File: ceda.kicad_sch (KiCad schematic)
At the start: 0 parts

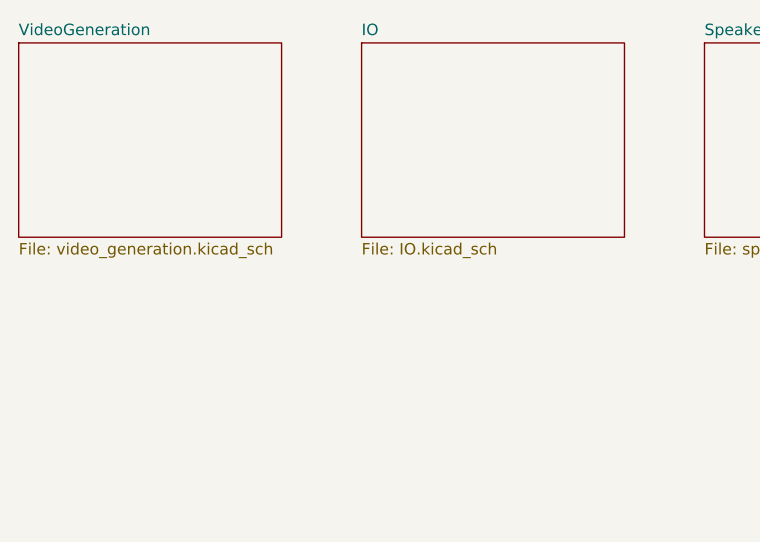
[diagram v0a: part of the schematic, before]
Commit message: Embed new sheets and fix symbols.
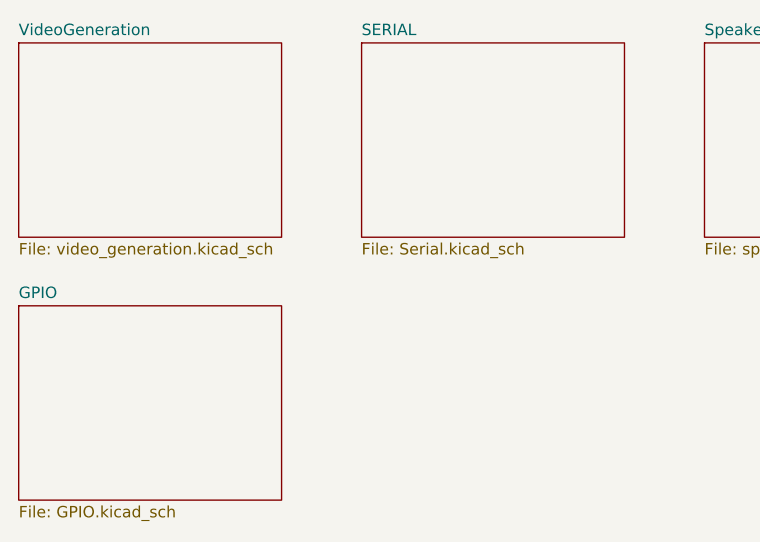
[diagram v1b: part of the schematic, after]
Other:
- sheet IO renamed SERIAL
- added sheet GPIO (GPIO.kicad_sch)
- sheet SERIAL: file IO.kicad_sch -> Serial.kicad_sch
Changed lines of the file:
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@@
+    )
+  )
+  (sheet (at 25.4 54.61) (size 29.21 21.59) (fields_autoplaced)
+    (stroke (width 0.1524) (type solid) (color 0 0 0 0))
+    (fill (color 0 0 0 0.0000))
+    (property "Sheet name" "GPIO" (id 0) (at 25.4 53.8984 0)
+      (effects (font (size 1.27 1.27)) (justify left bottom))
+    )
+    (property "Sheet file" "GPIO.kicad_sch" (id 1) (at 25.4 76.7846 0)
+      (effects (font (size 1.27 1.27)) (justify left top))
     )
   )
@@
     (stroke (width 0.1524) (type solid) (color 0 0 0 0))
     (fill (color 0 0 0 0.0000))
-    (property "Sheet name" "IO" (id 0) (at 63.5 24.6884 0)
+    (property "Sheet name" "SERIAL" (id 0) (at 63.5 24.6884 0)
       (effects (font (size 1.27 1.27)) (justify left bottom))
     )
-    (property "Sheet file" "IO.kicad_sch" (id 1) (at 63.5 47.5746 0)
+    (property "Sheet file" "Serial.kicad_sch" (id 1) (at 63.5 47.5746 0)
       (effects (font (size 1.27 1.27)) (justify left top))
     )
@@
     (path "/ef850a34-fb31-4ec2-8b90-4e6ea535ae17" (page "4"))
     (path "/1847fdc4-53d8-4940-8c5f-7a326599bae2" (page "5"))
+    (path "/23c42ab9-740a-4e84-88f1-9f74965e7273" (page "6"))
   )
   (symbol_instances
@@
       (reference "#PWR?") (unit 1) (value "GND") (footprint "")
     )
+    (path "/23c42ab9-740a-4e84-88f1-9f74965e7273/3eef50a5-c9f6-4380-8968-412e4e210646"
+      (reference "#PWR?") (unit 1) (value "GND") (footprint "")
+    )
     (path "/ce60e45b-d802-4380-8f39-bef3de5fa20e/44904acb-380f-449a-b553-049731fee477"
       (reference "#PWR?") (unit 1) (value "VCC") (footprint "")
@@
     (path "/ce60e45b-d802-4380-8f39-bef3de5fa20e/4f72cf7f-9018-4e80-b599-22f4012bbe5a"
       (reference "#PWR?") (unit 1) (value "VCC") (footprint "")
+    )
+    (path "/23c42ab9-740a-4e84-88f1-9f74965e7273/4f79b821-bb86-4a79-8cc9-a31ff99ad1b3"
+      (reference "#PWR?") (unit 1) (value "GND") (footprint "")
     )
     (path "/ef850a34-fb31-4ec2-8b90-4e6ea535ae17/526bc8fc-b9ea-4f6d-a11e-04b82edc0316"
@@
       (reference "#PWR?") (unit 1) (value "GND") (footprint "")
     )
+    (path "/23c42ab9-740a-4e84-88f1-9f74965e7273/81f6af90-205c-4009-9fca-95e76bc3a30c"
+      (reference "#PWR?") (unit 1) (value "GND") (footprint "")
+    )
     (path "/ce60e45b-d802-4380-8f39-bef3de5fa20e/8708e44f-744a-4c71-8d3e-9b33e5565dd3"
       (reference "#PWR?") (unit 1) (value "GND") (footprint "")
@@
     (path "/1847fdc4-53d8-4940-8c5f-7a326599bae2/ac0df0c0-bf3f-4c2e-9fcf-2dcb79aa226c"
       (reference "#PWR?") (unit 1) (value "GND") (footprint "")
+    )
+    (path "/23c42ab9-740a-4e84-88f1-9f74965e7273/acd3b74a-4ce0-4828-b235-d3353f238170"
+      (reference "#PWR?") (unit 1) (value "VCC") (footprint "")
     )
     (path "/ce60e45b-d802-4380-8f39-bef3de5fa20e/afa3161e-0796-4f88-bb71-3bac43397641"
@@
       (reference "#PWR?") (unit 1) (value "GND") (footprint "")
     )
+    (path "/23c42ab9-740a-4e84-88f1-9f74965e7273/be6090c6-9d5f-45e2-8095-8eb5a1703aa2"
+      (reference "#PWR?") (unit 1) (value "VCC") (footprint "")
+    )
     (path "/ef850a34-fb31-4ec2-8b90-4e6ea535ae17/bfe7a632-2cca-4194-b346-5928404f8228"
       (reference "#PWR?") (unit 1) (value "GND") (footprint "")
@@
       (reference "#PWR?") (unit 1) (value "GND") (footprint "")
     )
+    (path "/23c42ab9-740a-4e84-88f1-9f74965e7273/f7eb22af-aba2-4009-a993-e9895948b84e"
+      (reference "#PWR?") (unit 1) (value "VCC") (footprint "")
+    )
     (path "/ce60e45b-d802-4380-8f39-bef3de5fa20e/f9799c5d-8034-46e6-ad18-7f272051b29a"
       (reference "#PWR?") (unit 1) (value "VCC") (footprint "")
@@
     (path "/1847fdc4-53d8-4940-8c5f-7a326599bae2/fada5dd4-0d0e-47e0-a18d-0bc406ca8606"
       (reference "#PWR?") (unit 1) (value "VCC") (footprint "")
+    )
+    (path "/23c42ab9-740a-4e84-88f1-9f74965e7273/b4e68656-41c0-4812-b001-a90783a3a6bd"
+      (reference "B10-B14") (unit 1) (value "uPD8255") (footprint "")
     )
     (path "/e6a0e8fd-e32c-428e-9a73-cac8f5494d05/e3df07bf-3ffc-4940-820c-1edcc7f8802c"
@@
       (reference "E13") (unit 1) (value "74LS04") (footprint "")
     )
+    (path "/23c42ab9-740a-4e84-88f1-9f74965e7273/1d67d68b-66f8-4965-a562-05de77bcd7e5"
+      (reference "E13") (unit 2) (value "74LS04") (footprint "")
+    )
     (path "/ce60e45b-d802-4380-8f39-bef3de5fa20e/24d193cd-79a4-4ad8-8472-2b96f466d141"
       (reference "E13") (unit 4) (value "74LS04") (footprint "")
     )
+    (path "/23c42ab9-740a-4e84-88f1-9f74965e7273/24147921-68ae-4eb7-94fb-991f083e4eb0"
+      (reference "E14") (unit 2) (value "74LS74") (footprint "")
+    )
     (path "/1847fdc4-53d8-4940-8c5f-7a326599bae2/4f4ed95e-9189-46b4-888b-34cae86c7a4c"
       (reference "F2-F5") (unit 1) (value "Z80CPU") (footprint "")
@@
       (reference "F10") (unit 1) (value "74LS157") (footprint "")
     )
+    (path "/23c42ab9-740a-4e84-88f1-9f74965e7273/b2cb7d22-ca6e-4a29-949e-c29c143ac78c"
+      (reference "F13") (unit 2) (value "74LS08") (footprint "")
+    )
+    (path "/23c42ab9-740a-4e84-88f1-9f74965e7273/2f3af18b-1450-45cc-b2c4-93c8e85c8548"
+      (reference "F13") (unit 3) (value "74LS08") (footprint "")
+    )
+    (path "/23c42ab9-740a-4e84-88f1-9f74965e7273/03a4a81b-4d50-433c-ac26-4ba879c2eeff"
+      (reference "F14") (unit 2) (value "74LS00") (footprint "")
+    )
+    (path "/23c42ab9-740a-4e84-88f1-9f74965e7273/4ce003b7-7093-412b-af0a-951a986e5231"
+      (reference "F14") (unit 3) (value "74LS00") (footprint "")
+    )
+    (path "/23c42ab9-740a-4e84-88f1-9f74965e7273/c182f1fe-96b2-41c4-9f23-e8cec8bd9e21"
+      (reference "F14") (unit 4) (value "74LS00") (footprint "")
+    )
     (path "/ce60e45b-d802-4380-8f39-bef3de5fa20e/5f190ef2-1902-4f45-a247-a0f33f417382"
       (reference "H8H10") (unit 1) (value "uPD446") (footprint "")
     )
+    (path "/23c42ab9-740a-4e84-88f1-9f74965e7273/837dc2df-09af-4d71-9a02-297b79a158e0"
+      (reference "H9") (unit 1) (value "uPD446") (footprint "")
+    )
     (path "/ce60e45b-d802-4380-8f39-bef3de5fa20e/626b8579-fdf0-471a-93e7-d48f3b78ace4"
       (reference "H11") (unit 1) (value "74LS273") (footprint "")
@@
       (reference "H12H14") (unit 1) (value "2732") (footprint "")
     )
+    (path "/23c42ab9-740a-4e84-88f1-9f74965e7273/88ee6807-a5cd-4e50-9da6-34d72ca7c3ae"
+      (reference "J9") (unit 1) (value "uPD446") (footprint "")
+    )
     (path "/ce60e45b-d802-4380-8f39-bef3de5fa20e/1345e9a3-3879-41b5-b386-9d3dc565dea0"

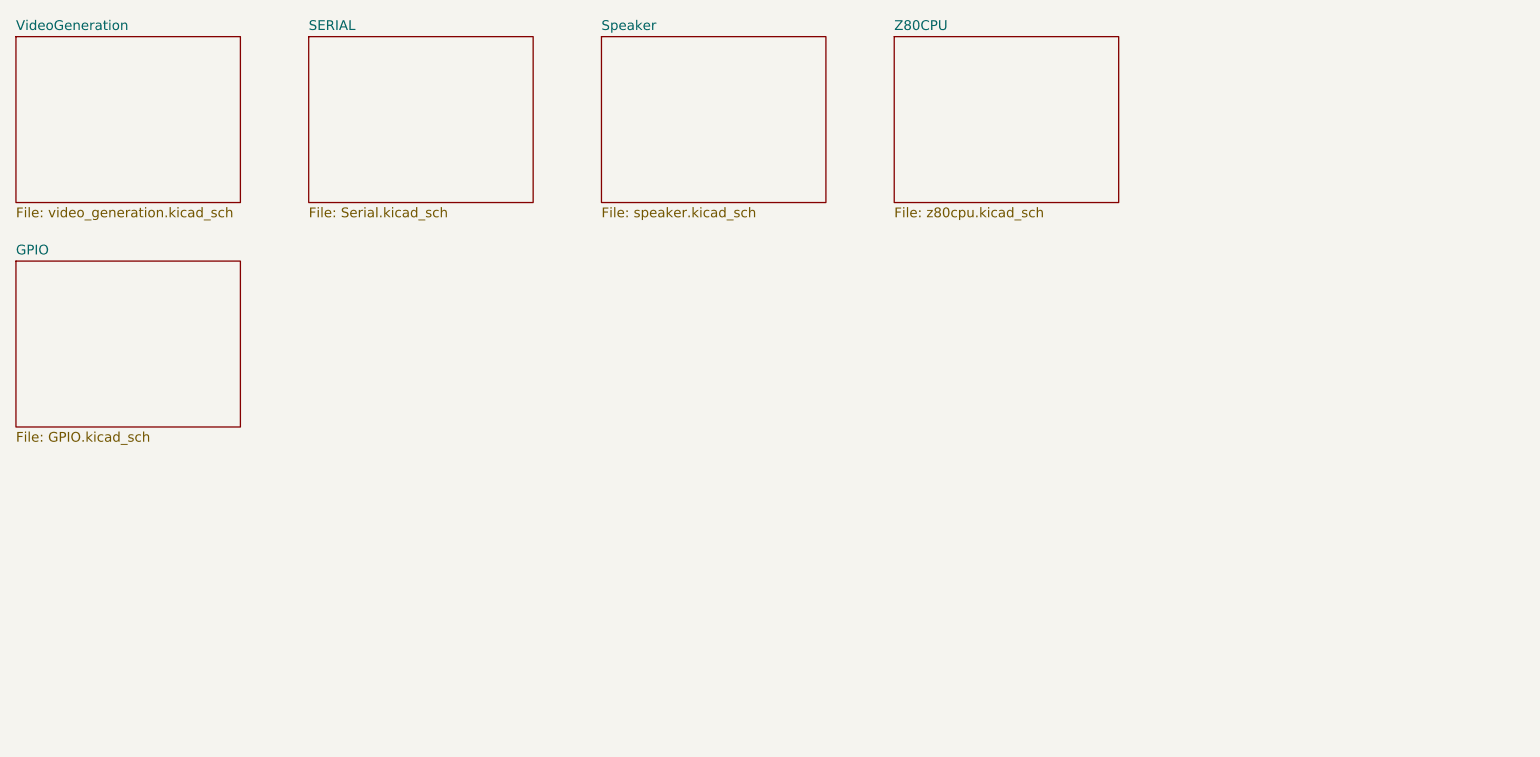
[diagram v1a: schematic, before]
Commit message: Add daughterboard schematics.
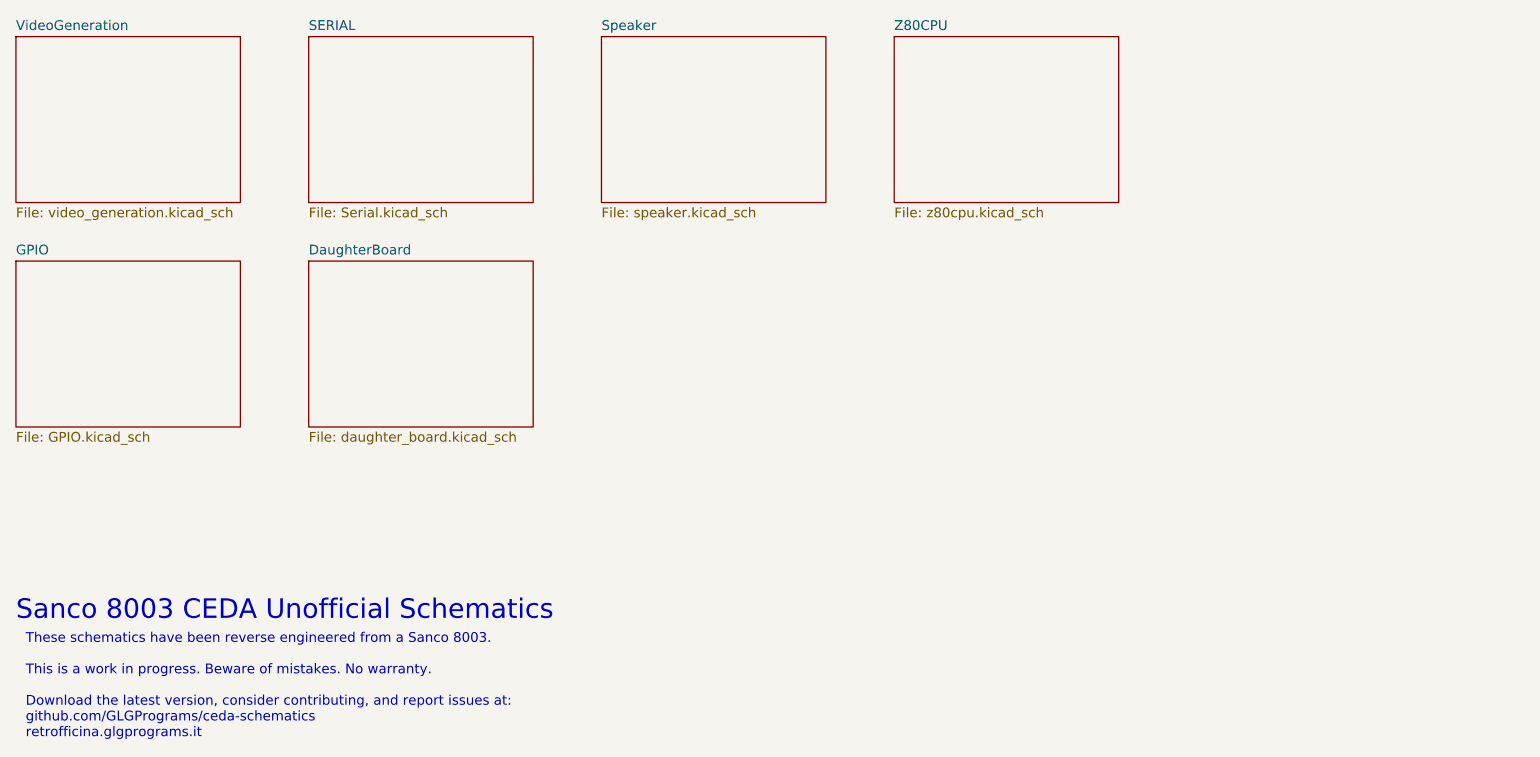
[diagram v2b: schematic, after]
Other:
- added sheet DaughterBoard (daughter_board.kicad_sch)
- note added: "Sanco 8003 CEDA Unofficial Schematics"
- note added: "These schematics have been reverse engineered from a Sanco 8003. This is a work in progress. Beware of mistakes. No warranty. Download the latest version, consider contributing, and report issues at: github.com/GLGPrograms/ceda-schematics retrofficina.glgprograms.it"
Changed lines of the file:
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@@
     (company "Logic Systems Int'l Inc")
   )
+  (text "These schematics have been reverse engineered from a Sanco 8003.\n\nThis is a work in progress. Beware of mistakes. No warranty.\n\nDownload the latest version, consider contributing, and report issues at:\ngithub.com/GLGPrograms/ceda-schematics\nretrofficina.glgprograms.it\n"
+    (at 26.67 116.84 0)
+    (effects (font (size 1.27 1.27)) (justify left bottom))
+  )
+  (text "Sanco 8003 CEDA Unofficial Schematics" (at 25.4 101.6 0)
+    (effects (font (size 2.54 2.54)) (justify left bottom))
+  )
   (sheet (at 139.7 25.4) (size 29.21 21.59) (fields_autoplaced)
     (stroke (width 0.1524) (type solid) (color 0 0 0 0))
@@
     )
     (property "Sheet file" "GPIO.kicad_sch" (id 1) (at 25.4 76.7846 0)
+      (effects (font (size 1.27 1.27)) (justify left top))
+    )
+  )
+  (sheet (at 63.5 54.61) (size 29.21 21.59) (fields_autoplaced)
+    (stroke (width 0.1524) (type solid) (color 0 0 0 0))
+    (fill (color 0 0 0 0.0000))
+    (property "Sheet name" "DaughterBoard" (id 0) (at 63.5 53.8984 0)
+      (effects (font (size 1.27 1.27)) (justify left bottom))
+    )
+    (property "Sheet file" "daughter_board.kicad_sch" (id 1) (at 63.5 76.7846 0)
       (effects (font (size 1.27 1.27)) (justify left top))
     )
@@
     (path "/1847fdc4-53d8-4940-8c5f-7a326599bae2" (page "5"))
     (path "/23c42ab9-740a-4e84-88f1-9f74965e7273" (page "6"))
+    (path "/4f1cc97c-1ae7-488a-96b4-ad54fee0fde4" (page "7"))
   )
   (symbol_instances
@@
       (reference "#PWR?") (unit 1) (value "+5V") (footprint "")
     )
+    (path "/4f1cc97c-1ae7-488a-96b4-ad54fee0fde4/3b12c81f-af2a-4545-b47f-dc7e2eccd6fa"
+      (reference "#PWR?") (unit 1) (value "VCC") (footprint "")
+    )
     (path "/1847fdc4-53d8-4940-8c5f-7a326599bae2/3bf4194b-f9e0-4505-8c24-68f9aad2fbc3"
       (reference "#PWR?") (unit 1) (value "GND") (footprint "")
@@
       (reference "#PWR?") (unit 1) (value "GND") (footprint "")
     )
+    (path "/4f1cc97c-1ae7-488a-96b4-ad54fee0fde4/43f7d1da-dc41-4737-81e0-b5bb678885e3"
+      (reference "#PWR?") (unit 1) (value "GND") (footprint "")
+    )
     (path "/ce60e45b-d802-4380-8f39-bef3de5fa20e/44904acb-380f-449a-b553-049731fee477"
       (reference "#PWR?") (unit 1) (value "VCC") (footprint "")
@@
       (reference "#PWR?") (unit 1) (value "VCC") (footprint "")
     )
+    (path "/4f1cc97c-1ae7-488a-96b4-ad54fee0fde4/4d2c484e-3a46-4211-852c-d4b4069e05ce"
+      (reference "#PWR?") (unit 1) (value "VCC") (footprint "")
+    )
+    (path "/4f1cc97c-1ae7-488a-96b4-ad54fee0fde4/4de7529a-3ebb-492a-9d76-afc139699f2f"
+      (reference "#PWR?") (unit 1) (value "GND") (footprint "")
+    )
     (path "/ce60e45b-d802-4380-8f39-bef3de5fa20e/4f72cf7f-9018-4e80-b599-22f4012bbe5a"
       (reference "#PWR?") (unit 1) (value "VCC") (footprint "")
@@
     (path "/ef850a34-fb31-4ec2-8b90-4e6ea535ae17/526bc8fc-b9ea-4f6d-a11e-04b82edc0316"
       (reference "#PWR?") (unit 1) (value "VCC") (footprint "")
+    )
+    (path "/4f1cc97c-1ae7-488a-96b4-ad54fee0fde4/543e8ccc-3615-4145-bcbd-e34b509dad93"
+      (reference "#PWR?") (unit 1) (value "GND") (footprint "")
     )
     (path "/ce60e45b-d802-4380-8f39-bef3de5fa20e/5692bd57-cbe9-40b8-9758-0208a16e232d"
@@
       (reference "#PWR?") (unit 1) (value "VCC") (footprint "")
     )
+    (path "/4f1cc97c-1ae7-488a-96b4-ad54fee0fde4/660c367a-ab78-4ce1-a53d-7b9ba1fb04c6"
+      (reference "#PWR?") (unit 1) (value "VCC") (footprint "")
+    )
     (path "/ce60e45b-d802-4380-8f39-bef3de5fa20e/678d3c66-71fc-45a9-b0f2-ab57654e5cd6"
       (reference "#PWR?") (unit 1) (value "VCC") (footprint "")
@@
     )
     (path "/ef850a34-fb31-4ec2-8b90-4e6ea535ae17/9f0cf96d-478c-4448-8f14-dd0641c3ca72"
+      (reference "#PWR?") (unit 1) (value "VCC") (footprint "")
+    )
+    (path "/4f1cc97c-1ae7-488a-96b4-ad54fee0fde4/9fe5da37-f255-43aa-869a-cd0e477981eb"
       (reference "#PWR?") (unit 1) (value "VCC") (footprint "")
     )
@@
       (reference "#PWR?") (unit 1) (value "GND") (footprint "")
     )
+    (path "/4f1cc97c-1ae7-488a-96b4-ad54fee0fde4/ded65276-3aff-429b-a416-9a56842861af"
+      (reference "#PWR?") (unit 1) (value "GND") (footprint "")
+    )
     (path "/ce60e45b-d802-4380-8f39-bef3de5fa20e/e2355411-fdf7-46b8-b4cf-baec94c212c8"
       (reference "#PWR?") (unit 1) (value "GND") (footprint "")
@@
     (path "/ce60e45b-d802-4380-8f39-bef3de5fa20e/edaa7e6b-ed01-46be-bf67-d9109d8c5c4b"
       (reference "#PWR?") (unit 1) (value "GND") (footprint "")
+    )
+    (path "/4f1cc97c-1ae7-488a-96b4-ad54fee0fde4/ef73e9b1-faca-4bc0-97e5-2e34798557ae"
+      (reference "#PWR?") (unit 1) (value "VCC") (footprint "")
     )
     (path "/ef850a34-fb31-4ec2-8b90-4e6ea535ae17/f5af1971-e234-4870-aeaf-efe7b55386b6"
@@
       (reference "J15") (unit 1) (value "74LS161") (footprint "")
     )
+    (path "/4f1cc97c-1ae7-488a-96b4-ad54fee0fde4/13731206-be3f-489c-88a5-7dfe5c5b4ba8"
+      (reference "J?") (unit 1) (value "Conn_02x25_Odd_Even") (footprint "")
+    )
     (path "/e6a0e8fd-e32c-428e-9a73-cac8f5494d05/24e14e3c-564f-46d1-97db-c614eb7871fd"
       (reference "J?") (unit 1) (value "SIOCLK") (footprint "")
     )
-    (path "/e6a0e8fd-e32c-428e-9a73-cac8f5494d05/b1f729a5-eca0-4413-bc71-3c76f3db5d0d"
-      (reference "J?") (unit 1) (value "Conn_02x25_Odd_Even") (footprint "")
-    )
     (path "/ce60e45b-d802-4380-8f39-bef3de5fa20e/e582a31c-3ec3-45a4-97da-704124c96bfc"
       (reference "J?") (unit 1) (value "Conn_02x06_Odd_Even") (footprint "")
@@
       (reference "K15") (unit 4) (value "74LS04") (footprint "")
     )
+    (path "/4f1cc97c-1ae7-488a-96b4-ad54fee0fde4/006b1c0c-99fc-45cf-ae28-0f109fcc0f52"
+      (reference "KEYBOARD") (unit 1) (value "DIN-8") (footprint "")
+    )
     (path "/ce60e45b-d802-4380-8f39-bef3de5fa20e/a94137ef-cbc6-42c4-bf1f-2c8952a4a8f9"
       (reference "L13") (unit 1) (value "74LS38") (footprint "")
@@
       (reference "LS0") (unit 1) (value "Speaker") (footprint "")
     )
+    (path "/4f1cc97c-1ae7-488a-96b4-ad54fee0fde4/080b93d1-2825-4343-812f-bbef33a831da"
+      (reference "PRINTER") (unit 1) (value "PRINTER") (footprint "")
+    )
+    (path "/4f1cc97c-1ae7-488a-96b4-ad54fee0fde4/fb1f5312-67fd-4bb9-9338-3f4d343b565f"
+      (reference "PRNT") (unit 1) (value "DIN-5_180degree") (footprint "")
+    )
     (path "/ce60e45b-d802-4380-8f39-bef3de5fa20e/a0785fe0-4575-4fb3-a3ae-36bdc4ccec94"
       (reference "Q?") (unit 1) (value "Q_NPN_BCE") (footprint "")
@@
       (reference "R79") (unit 1) (value "4k7") (footprint "")
     )
+    (path "/4f1cc97c-1ae7-488a-96b4-ad54fee0fde4/9128c703-0d08-4b42-9d41-a2c8a178fd2b"
+      (reference "R?") (unit 1) (value "470R") (footprint "")
+    )
+    (path "/4f1cc97c-1ae7-488a-96b4-ad54fee0fde4/d2eb51d4-8a4a-40a5-afe3-747bdb0579ca"
+      (reference "R?") (unit 1) (value "470R") (footprint "")
+    )
     (path "/ce60e45b-d802-4380-8f39-bef3de5fa20e/751ea553-10b6-4bcf-a8bf-5eabcf2623d3"
       (reference "RCK") (unit 1) (value "ContrastKnob") (footprint "")
     )
+    (path "/4f1cc97c-1ae7-488a-96b4-ad54fee0fde4/20942738-9a37-4901-a8f1-f2f78c1b1574"
+      (reference "SCLK") (unit 1) (value "Jumper_2_Bridged") (footprint "")
+    )
+    (path "/4f1cc97c-1ae7-488a-96b4-ad54fee0fde4/90d2f535-4006-4c9e-804a-d97cfa86159b"
+      (reference "SERIAL") (unit 1) (value "DB25_Female") (footprint "")
+    )
     (path "/ef850a34-fb31-4ec2-8b90-4e6ea535ae17/63a8299c-2ac2-4637-b1df-0f022bdb4485"

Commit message: Added memory management sheet with ROM/RAM addressing mux
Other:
- added sheet MainMemoryManagement (main_memory_management.kicad_sch)
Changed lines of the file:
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@@
+    )
+  )
+  (sheet (at 101.6 54.61) (size 29.21 21.59) (fields_autoplaced)
+    (stroke (width 0.1524) (type solid))
+    (fill (color 0 0 0 0.0000))
+    (property "Sheetname" "MainMemoryManagement" (at 101.6 53.8984 0)
+      (effects (font (size 1.27 1.27)) (justify left bottom))
+    )
+    (property "Sheetfile" "main_memory_management.kicad_sch" (at 101.6 76.7846 0)
+      (effects (font (size 1.27 1.27)) (justify left top))
+    )
+    (property "Campo2" "" (at 101.6 54.61 0)
+      (effects (font (size 1.27 1.27)) hide)
+    )
+    (instances
+      (project "ceda"
+        (path "/12a6dbe3-008d-4c5b-88f6-9f1c816060be" (page "8"))
+      )
     )
   )

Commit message: RAM addressing, including DRAM ras and cas
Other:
- added sheet DRAM and parity (dram.kicad_sch)
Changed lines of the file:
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@@
+    )
+  )
+  (sheet (at 139.7 54.61) (size 29.21 21.59) (fields_autoplaced)
+    (stroke (width 0.1524) (type solid))
+    (fill (color 0 0 0 0.0000))
+    (property "Sheetname" "DRAM and parity" (at 139.7 53.8984 0)
+      (effects (font (size 1.27 1.27)) (justify left bottom))
+    )
+    (property "Sheetfile" "dram.kicad_sch" (at 139.7 76.7846 0)
+      (effects (font (size 1.27 1.27)) (justify left top))
+    )
+    (property "Campo2" "" (at 139.7 54.61 0)
+      (effects (font (size 1.27 1.27)) hide)
+    )
+    (instances
+      (project "ceda"
+        (path "/12a6dbe3-008d-4c5b-88f6-9f1c816060be" (page "9"))
+      )
     )
   )
